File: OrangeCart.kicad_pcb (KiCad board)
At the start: 6 copper layers, 62 x 50 mm, 136 parts, among them J1 Conn_02x11_Odd_Even, J3 USB_B_Mini, J4 MicroSd, J6 JTAG, SW1 SW_Push, U1 FAN53541, U10 NCP115-2.5, U11 74AHCV17A, U12 74LVC3G17, U13 SN74LVC8T245, U14 SN74LVC8T245, U2 FAN53541, U3 LFE5U-25F-8BG256C, U4 S70KS1281, U5 74LVC06A, U6 W25Q128JVP, U7 FAN53541, U8 74LVC1G06, U9 SN74LVC8T245, X1 EXPANSION_PORT_C64_EDGE

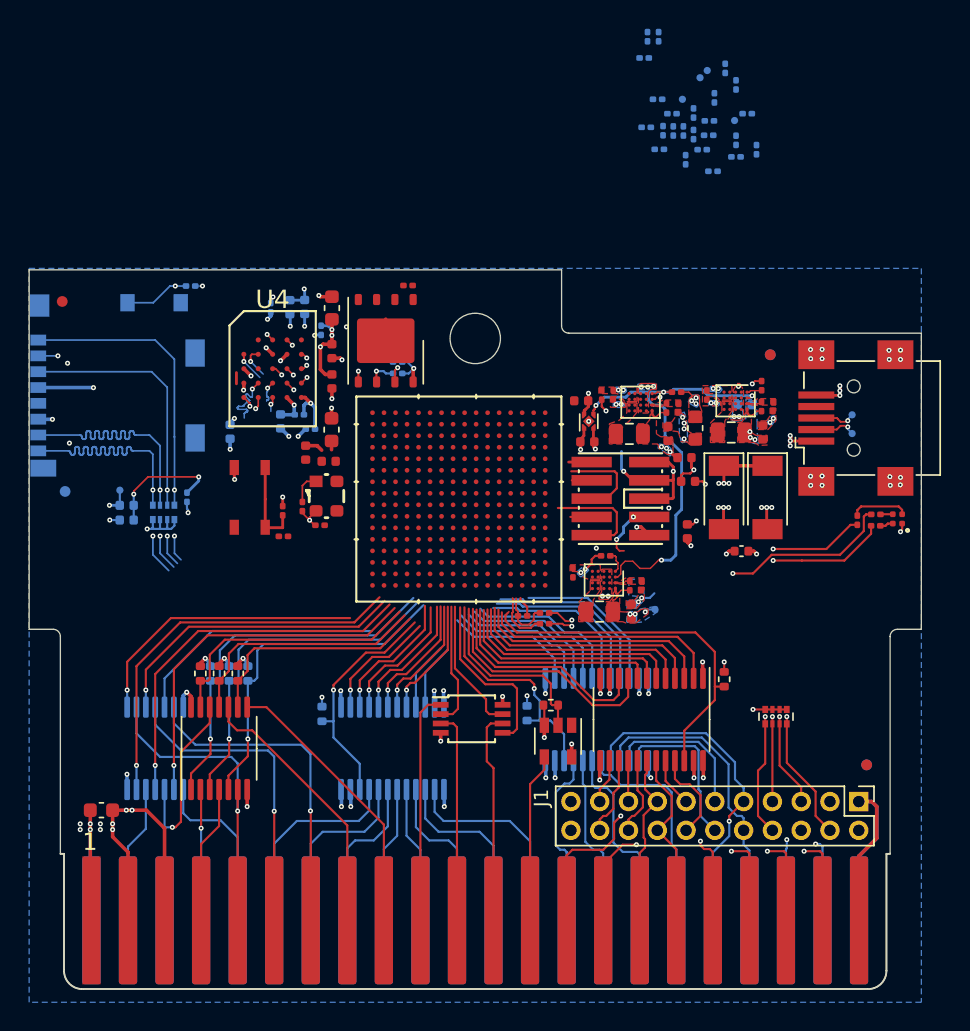
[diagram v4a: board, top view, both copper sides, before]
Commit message: Increase via size
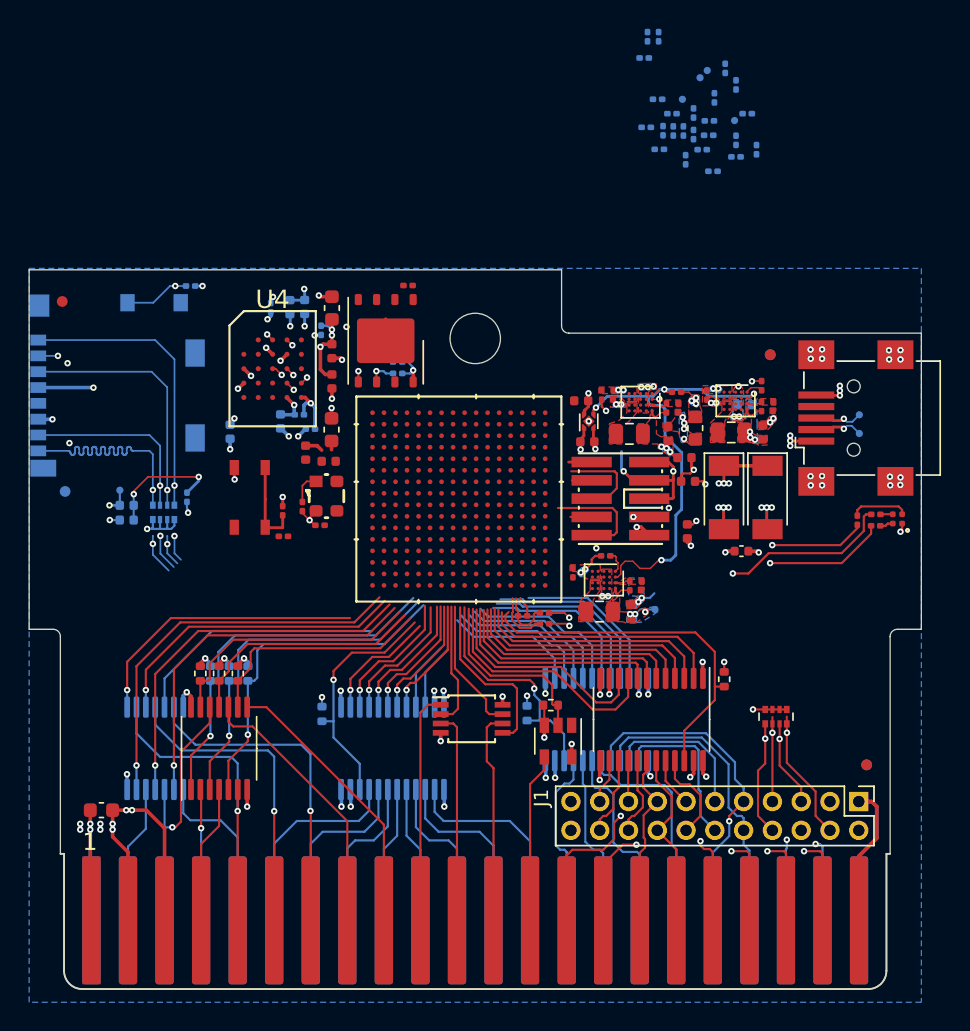
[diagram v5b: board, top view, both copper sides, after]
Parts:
- moved TP26 0.50 mm to (106.7, 90.2)
- moved TP27 0.50 mm to (106.7, 91.5)
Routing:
- net QSPI_D3: track 8.90 -> 0.00 mm, vias 1 -> 0
- net SD0_DAT0: track 24.0 -> 19.0 mm
- net RAM_DQ1: track 4.77 -> 0.00 mm, vias 1 -> 0
- net GND: track 108.3 -> 104.4 mm, vias 92 -> 91
- net RAM_CK+: track 2.22 -> 0.00 mm, vias 1 -> 0
- net RAM_CK-: track 2.12 -> 0.05 mm, vias 1 -> 0
- net RAM_DQ0: track 1.56 -> 0.00 mm, vias 1 -> 0
- net /sheetIO/_USB_D_P: track 35.8 -> 37.0 mm
- net CSPARECS: track 36.9 -> 38.0 mm
- net CIORD: track 32.7 -> 33.8 mm
- net CRTCCS: track 33.7 -> 34.7 mm
- net CIOWR: track 35.6 -> 36.6 mm
- net RAM_DQ5: track 1.02 -> 0.00 mm, vias 1 -> 0
- net /sheetIO/_USB_D_N: track 35.9 -> 36.9 mm
- net RAM_DQ6: track 0.85 -> 0.00 mm, vias 1 -> 0
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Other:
- net class DDR3_CTRL_LM1.0 removed
- net class DDR3_DQS0_LM1.0 removed
- net class DDR3_DQS1_LM1.0 removed
- net class DDR_CLK_LM1.0 removed
- net class Default: clearance 0.0635 -> 0.1016; trace_width 0.0889 -> 0.127; via_dia 0.6 -> 0.45; via_drill 0.4 -> 0.2
- rule trace_clearance: 0.0635 -> 0.1016
- rule trace_min: 0.0889 -> 0.1016
- rule via_min_size: 0.35 -> 0.45

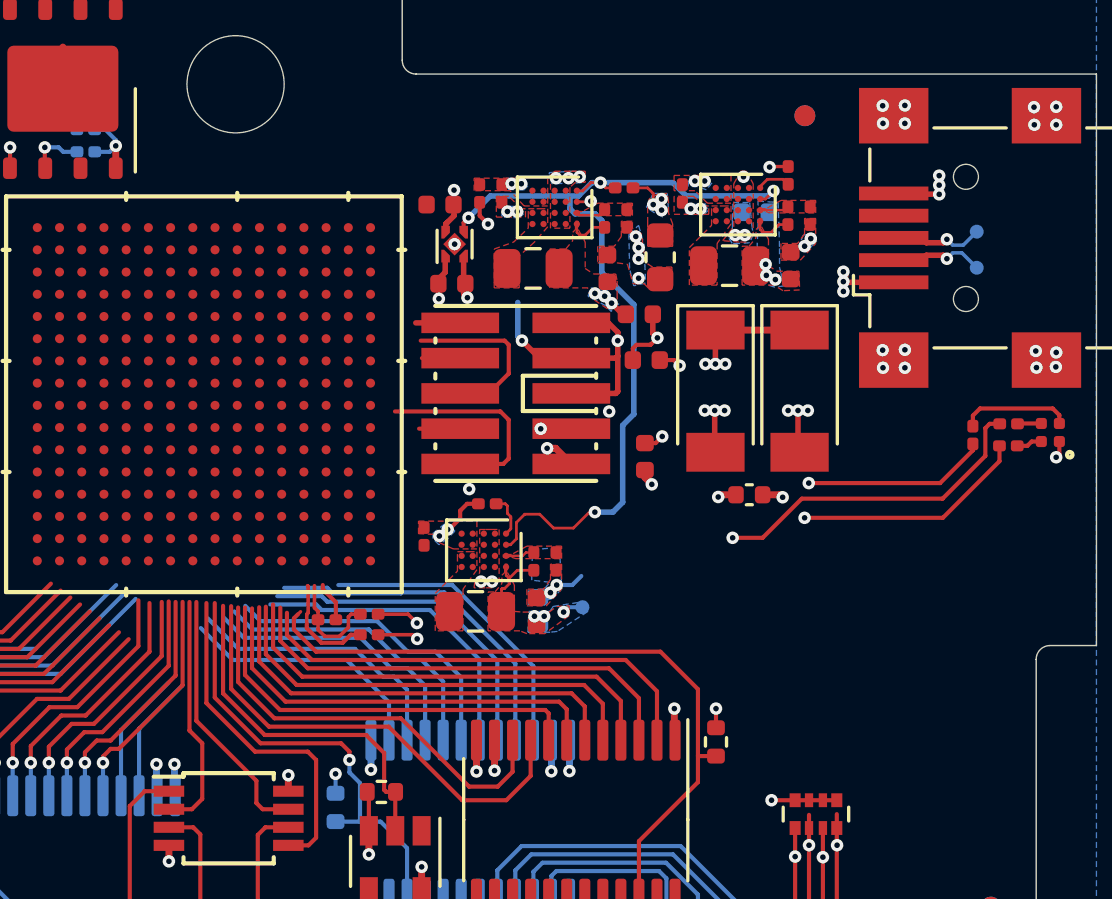
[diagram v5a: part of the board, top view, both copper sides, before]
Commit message: Fix remaining DRC violations after dimension changes
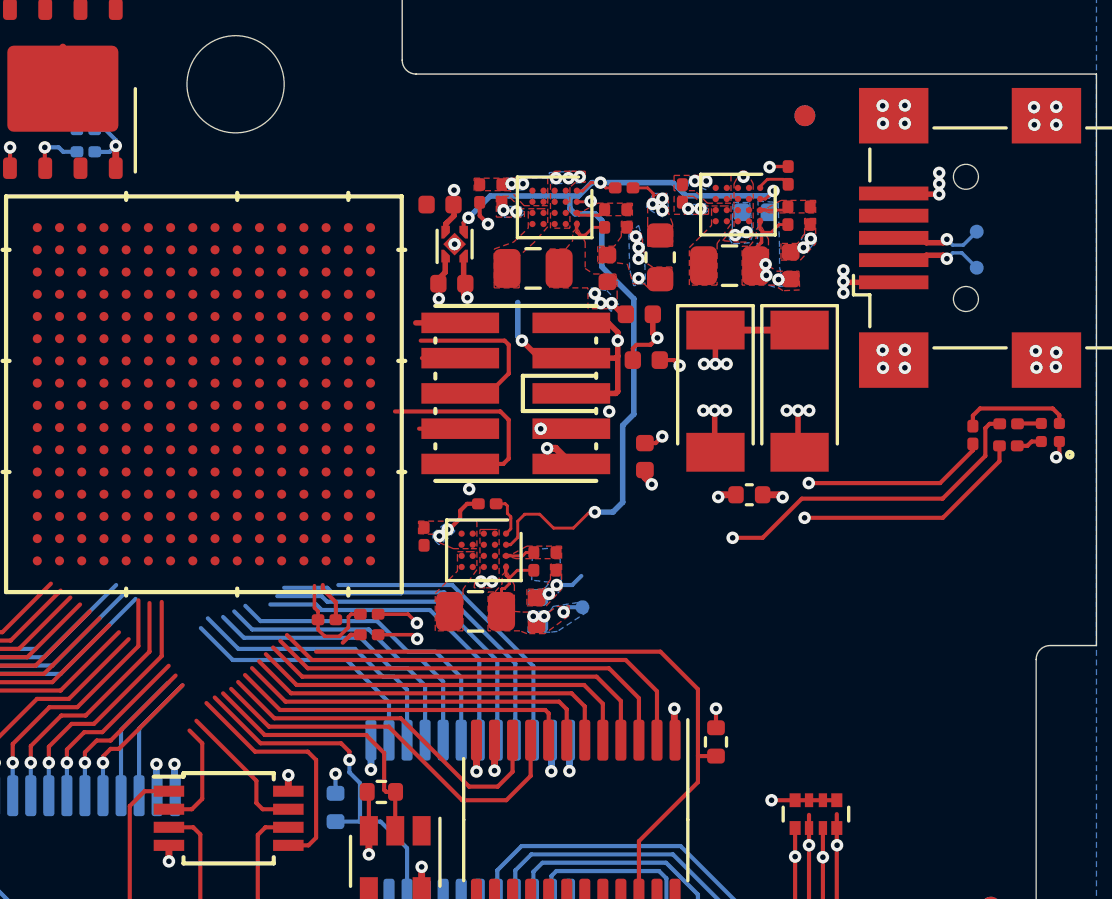
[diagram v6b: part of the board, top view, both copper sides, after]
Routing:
- net BA: track 8.64 -> 4.01 mm
- net IO2: track 9.38 -> 5.10 mm
- net ROML: track 12.3 -> 8.71 mm
- net A_~EN~_L: track 16.5 -> 13.1 mm
- net DMA: track 13.0 -> 9.86 mm
- net USB_D-: track 3.83 -> 0.75 mm
- net A10: track 8.34 -> 5.34 mm
- net D0: track 17.1 -> 14.1 mm
- net D1: track 15.5 -> 12.8 mm
- net A11: track 8.62 -> 5.97 mm
- net D3: track 14.9 -> 12.5 mm
- net A12: track 8.90 -> 6.58 mm
- net D2: track 15.2 -> 13.1 mm
- net D5: track 15.6 -> 13.6 mm
- net D_~EN: track 25.3 -> 23.4 mm
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
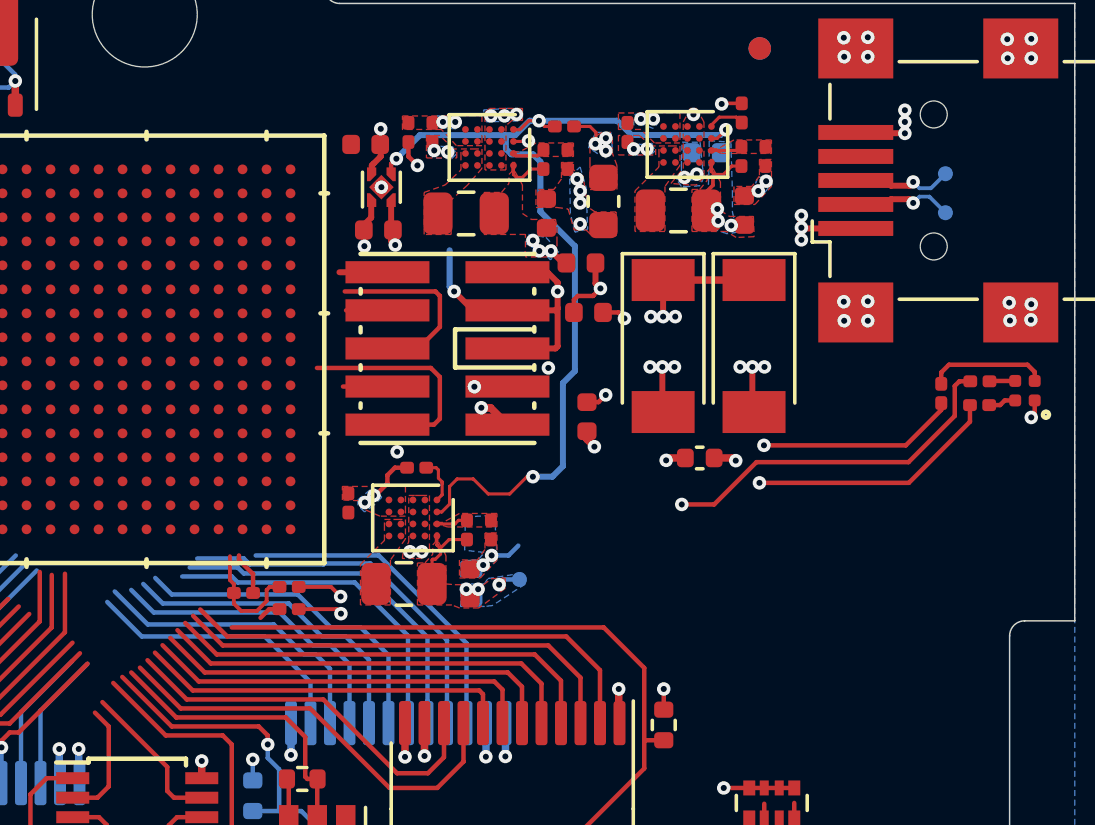
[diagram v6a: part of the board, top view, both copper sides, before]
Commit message: Move USB tracks
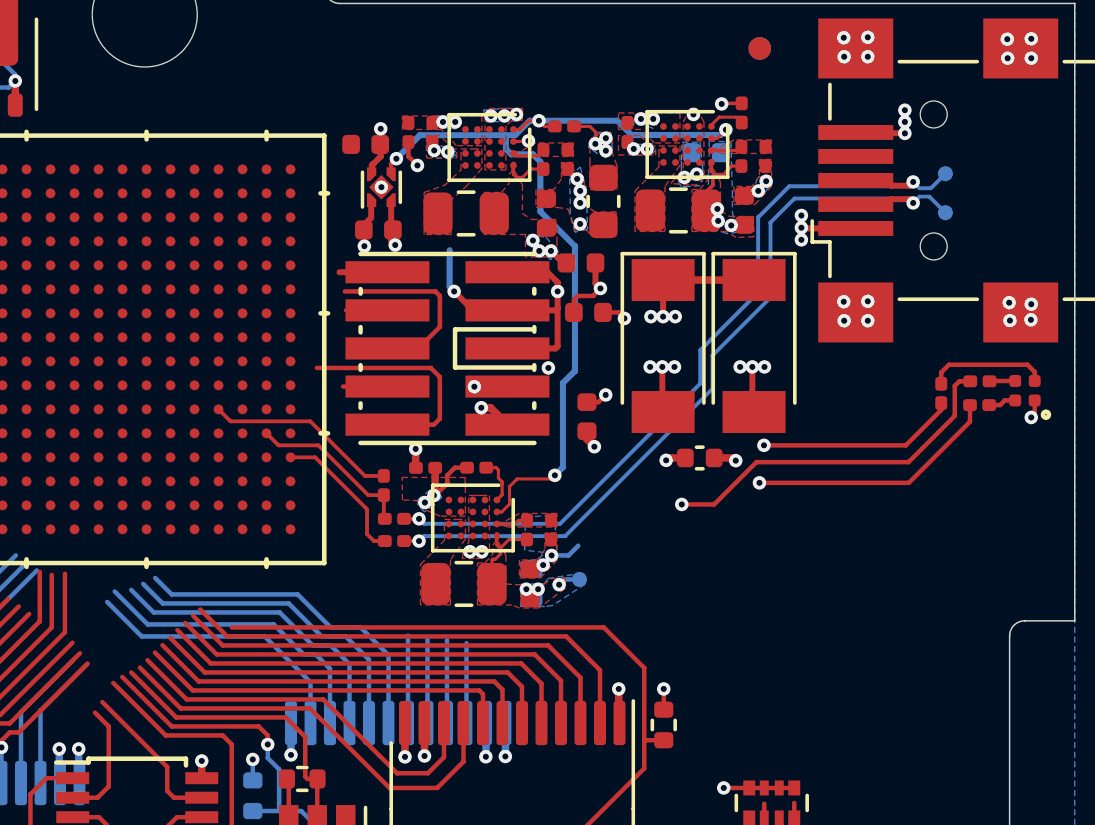
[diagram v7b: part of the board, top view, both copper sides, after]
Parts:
- moved R20 5.89 mm to (88.0, 100.6), turned to 90 degrees
- moved R21 4.18 mm to (88.3, 101.7)
- moved R29 4.18 mm to (88.3, 102.4)
- moved C14 2.83 mm to (89.4, 100.0), turned to 0 degrees
- moved C16 2.00 mm to (92.9, 103.8)
- moved C18 2.00 mm to (92.8, 103.8)
- moved L3 2.00 mm to (90.6, 103.8)
- moved R14 2.00 mm to (91.1, 100.0)
- moved R16 2.00 mm to (93.5, 102.0)
- moved R18 2.00 mm to (92.7, 102.0)
- moved TP31 2.00 mm to (94.5, 103.7)
- moved U7 2.00 mm to (90.9, 101.6)
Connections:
- U3 pad M12: USB_D- -> Net-(U3-PadM12)
- U3 pad N12: USB_PULLUP -> Net-(U3-PadN12)
- U3 pad N6: Net-(U3-PadN6) -> USB_PULLUP
- U3 pad P12: USB_D+ -> Net-(U3-PadP12)
- U3 pad R5: Net-(U3-PadR5) -> USB_D+
- U3 pad T4: Net-(U3-PadT4) -> USB_D-
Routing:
- net LED_R: track 23.3 -> 8.42 mm
- net LED_B: track 21.1 -> 6.63 mm
- net LED_G: track 23.4 -> 11.9 mm
- net /sheetIO/_USB_D_P: track 37.0 -> 27.3 mm
- net /sheetIO/_USB_D_N: track 36.9 -> 27.3 mm
- net A1: track 12.2 -> 2.76 mm
- net A2: track 11.8 -> 2.86 mm
- net A3: track 11.3 -> 2.91 mm
- net A0: track 10.9 -> 2.66 mm
- net USB_PULLUP: track 1.44 -> 6.43 mm
- net VSYS: track 38.0 -> 33.9 mm
- net USB_D-: track 0.75 -> 4.78 mm
- net /sheetPower/PGOOD_P1.1V: track 32.9 -> 30.5 mm
- net USB_D+: track 3.81 -> 5.57 mm
- net GND: track 103.9 -> 104.6 mm

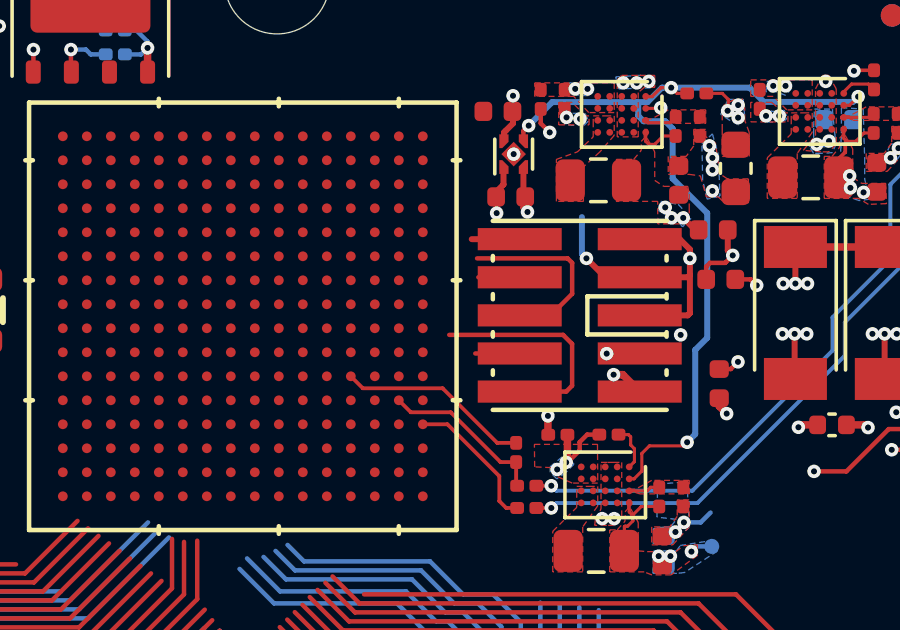
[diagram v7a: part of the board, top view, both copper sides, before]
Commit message: Reconnect JTAG
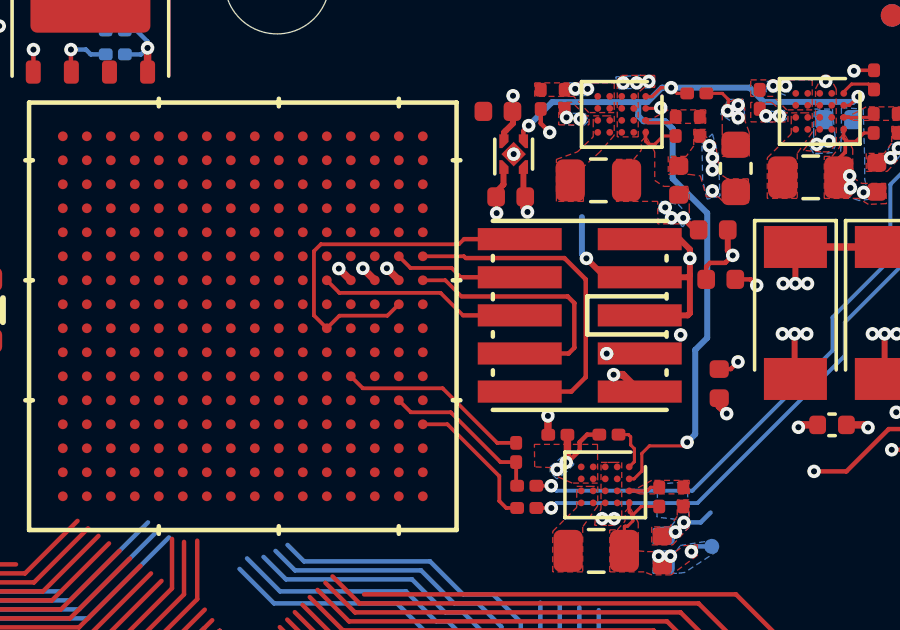
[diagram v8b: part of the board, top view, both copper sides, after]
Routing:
- net FPGA_RESET: track 1.60 -> 12.5 mm
- net JTAG_TCK: track 1.48 -> 8.75 mm
- net JTAG_TMS: track 7.44 -> 11.4 mm
- net JTAG_TDI: track 1.38 -> 4.32 mm
- net GND: track 104.6 -> 105.7 mm, vias 91 -> 93
- net JTAG_TDO: track 6.31 -> 6.91 mm
- net P3.3V: track 29.5 -> 30.1 mm, vias 20 -> 21
